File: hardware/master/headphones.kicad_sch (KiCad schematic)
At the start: 29 parts, among them J751 PHONES, K751 G6K-2F-Y DC12, U751 DG413DY, U752 TPA6120A2DWP

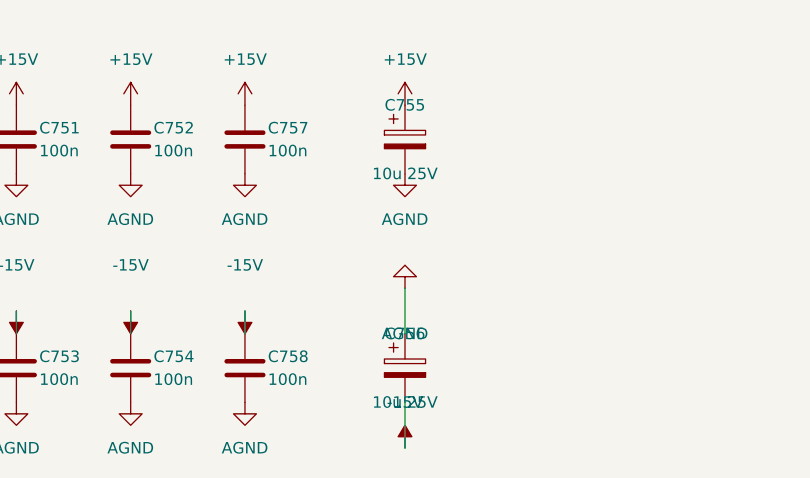
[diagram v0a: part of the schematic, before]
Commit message: Master card: DRV135 outputs, TL062 levers, SMD electrolytics, both raw rails watched (decisions 125-128)
/board master pre-layout session; the user delegated the open points.
- Confirms the [proposed] parts of decisions 89-94 (Q5 checked, +22 dB
  makeup kept for the breadboard, fallback R439 = 330k).
- 125: TI DRV135UA replaces the end-of-life THAT1646 (THAT memo
  2026-09-01); same SO-8 pinout, LCSC C544663.
- 126: U409, U410, U802, U804 TL072 -> TL062; superdiodes and U407 stay.
- 127: master electrolytics to SMD (decision 111 parts, 5.4 mm).
- 128: U707C watches -20V_RAW (22k6/100k), wired-OR with the +20 V trip.
- Würth fields on J101/J901, BAT54 LCSC C152458, G6K and header
  drawings checked, LCSC stock checked; budget 331/260 mA typical.
- parts.csv candidates for master pots and meter LEDs; lcsc_check.py
  handles MOhm.
ERC 0/0, all netlist checks 0 problems, reuse lint clean.

Co-Authored-By: Claude Opus 5.5 <noreply@anthropic.com>
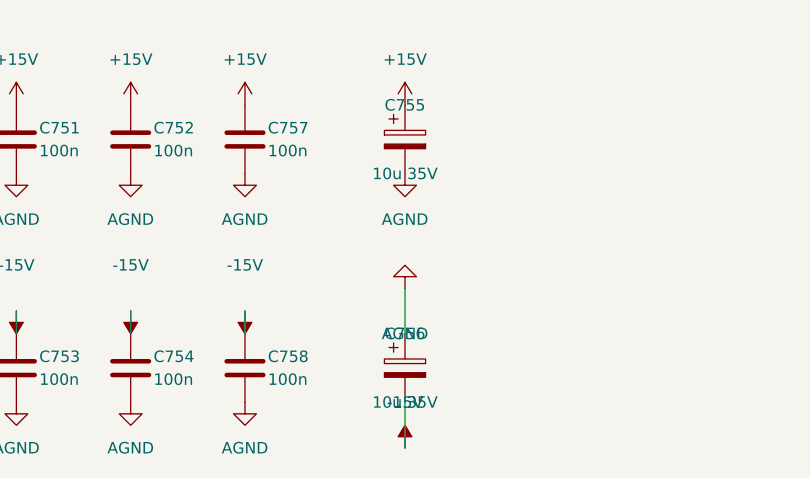
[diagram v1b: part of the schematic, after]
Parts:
- C755, C756: value 10u 25V -> 10u 35V; footprint Capacitor_THT:CP_Radial_D5.0mm_P2.00mm -> Capacitor_SMD:CP_Elec_5x5.4; MPN (none) -> RVT1V100M0505; Manufacturer (none) -> ROQANG; ProjectPN SX-C-012 -> SX-C-024; Supplier (none) -> LCSC; SupplierPN (none) -> C72486

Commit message: System: cost review and cost control (decisions 132-137)
Rean NYS216 jacks with a new footprint (132), through-hole parts hand-soldered (133), E24 values owned per board (134), live-device cost principle (135), /cost with the cost-controller sub-agent, tools/costs.py and a private ledger of realized costs (136), JLCPCB fee-free parts first (137).

Co-Authored-By: Claude Opus 5.5 <noreply@anthropic.com>
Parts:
- J751: footprint Connector_Audio:Jack_6.35mm_Neutrik_NMJ6HCD2_Horizontal -> syntsamix:Jack_6.35mm_Rean_NYS216_Horizontal; MPN NMJ6HCD2 -> NYS216; Manufacturer Neutrik -> Rean; ProjectPN SX-CONN-001 -> SX-CONN-015
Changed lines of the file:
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@@
 			)
 		)
-		(property "Footprint" "Connector_Audio:Jack_6.35mm_Neutrik_NMJ6HCD2_Horizontal"
+		(property "Footprint" "syntsamix:Jack_6.35mm_Rean_NYS216_Horizontal"
 			(at 233.68 43.18 0)
 			(hide yes)
@@
 			)
 		)
-		(property "ProjectPN" "SX-CONN-001"
+		(property "ProjectPN" "SX-CONN-015"
 			(at 233.68 43.18 0)
 			(hide yes)
@@
 			)
 		)
-		(property "Manufacturer" "Neutrik"
+		(property "Manufacturer" "Rean"
 			(at 233.68 43.18 0)
 			(hide yes)
@@
 			)
 		)
-		(property "MPN" "NMJ6HCD2"
+		(property "MPN" "NYS216"
 			(at 233.68 43.18 0)
 			(hide yes)

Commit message: Master card: fee-free parts and E24 values (decisions 144, 146-150)
- 144: AUX return and master fader laws on the channel's E24 pairs
- 146: meter ladder on fee-free E24 values (0.45 mA, within 0.14 dB); R732 22k + R737 560R
- 147: compressor R420/R426 E24 pairs, GR LED ladder 470k/4k3, SC LPF C503 2 x 47n C0G
  (Q 0.707, 44-478 Hz); TL072 symbols ST TL072CDT
- 148: AUX return receivers TL072 difference amplifiers (AD8273 gone from the project)
- 149: R421 plain 1k; compressor temperature compensation to the backlog
- 150: DG413, SSI2162, DRV135UA, AS3046D hand-soldered on the prototype master
  (symbol field Assembly, read by tools/costs.py); SPOF noted in the backlog
- Part swaps: button LEDs per colour, D504 BAT54W, D705-D712 1N4007W SOD-123FL,
  U641 DG411 -> DG413 with a Q601 inverter for send 1 (emitter on PGND, invariant 4)
- 70 -> 38 extended/consigned SMD types (about EUR 193 -> 105 per order);
  estimate EUR 794 / 1,074 / 1,671 for 4 / 8 / 16 channels
- Docs: STATUS, CONTINUE-FROM-HERE, ROADMAP backlog, SPEC, hardware/CLAUDE.md lessons

Co-Authored-By: Claude Opus 5.5 <noreply@anthropic.com>
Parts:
- U751: Assembly (none) -> hand (decision 150)

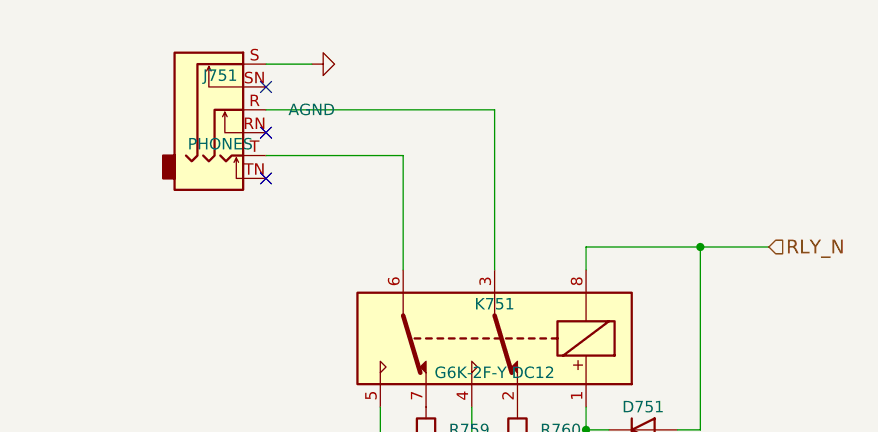
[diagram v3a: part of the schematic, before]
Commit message: Master: headphone jack, 0805 LEDs, off-board parts in the estimate (decisions 169-171)
- J751 becomes a KK 1x3 header for the panel Rean NYS230 with a ready-made
  Molex 217797-1031 lead (169)
- Master meter, gain-reduction (yellow) and PFL-active LEDs all 0805 basic
  parts; SX-D-005/006 retired (170)
- tools/costs.py counts parts without a schematic symbol from
  docs/costs/offboard.csv, and the two rear row-board PCBs (171):
  estimate EUR 831 / 1,110 / 1,693 for 4 / 8 / 16 channels
- New parts SX-CONN-019..022; ready-made input-module cable noted for /system
- NYS216/NYS230 samples to order; heatsink choice on hold (none fits 25 mm
  at decision 167's 57 C air), options in master STATUS

Co-Authored-By: Claude Opus 5.5 <noreply@anthropic.com>
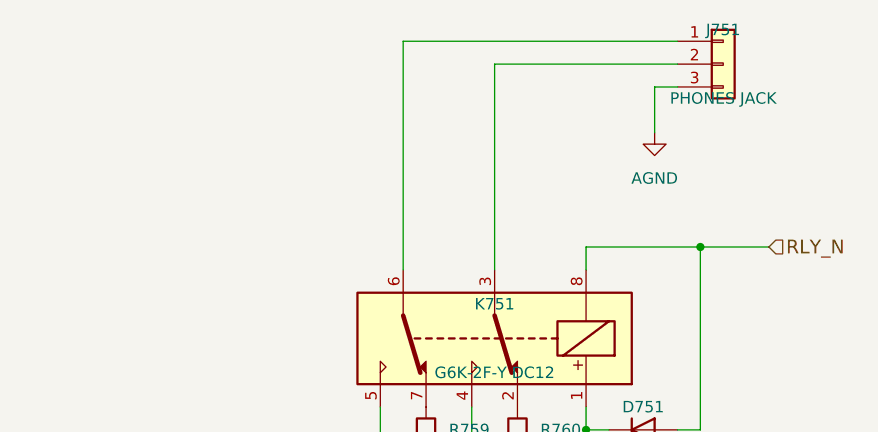
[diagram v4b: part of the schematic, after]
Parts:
- removed J751: PHONES, syntsamix:Jack_6.35mm_Rean_NYS216_Horizontal, symbol Connector_Audio:AudioJack3_Switch
- added J751: PHONES JACK, Connector_Molex:Molex_KK-254_AE-6410-03A_1x03_P2.54mm_Vertical, symbol Connector_Generic:Conn_01x03
- D752: footprint LED_THT:LED_D3.0mm -> LED_SMD:LED_0805_2012Metric; MPN (none) -> KT-0805Y; Manufacturer (none) -> Hubei KENTO; Note PFL active: lights while PFL_ACT is low -> PFL active: lights while PFL_ACT is low; 0805 under a print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; ProjectPN SX-D-005 -> SX-D-016; Supplier (none) -> LCSC; SupplierPN (none) -> C2296
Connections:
- net AGND: now also J751.3 (Pin_3)
- net at K751.3: now also J751.2 (Pin_2)
- net at K751.6: now also J751.1 (Pin_1)
- no-connect marks 3 -> 0
